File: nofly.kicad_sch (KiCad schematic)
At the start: 8 parts, among them J1 TYPE-C-31-M-12, J2 781710004, U1 USBLC6-2P6

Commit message: Finish wiring now?
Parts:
- J2: value 781710004 -> Conn_01x04_MountingPin; footprint acheron_Connectors:MOLEX_781710004 -> acheron_Connectors:MOLEX_PicoEZMate_781710004; symbol Connector_Generic:Conn_01x04 -> Connector_Generic_MountingPin:Conn_01x04_MountingPin
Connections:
- net GND: now also J2.MP (MountPin)
- no-connect marks 0 -> 2

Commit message: Some rerouting and checks
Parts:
- J2: value Conn_01x04_MountingPin -> 781710004
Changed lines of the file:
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@@
 		(dnp no)
 		(property "Reference" "R2"
-			(at 130.81 39.37 90)
+			(at 130.81 43.18 90)
 			(show_name no)
 			(do_not_autoplace no)
@@
 			(effects
 				(font
-					(size 0.508 0.508)
+					(size 0.762 0.762)
 				)
 			)
@@
 			)
 		)
-		(property "Value" "Conn_01x04_MountingPin"
-			(at 248.92 44.45 0)
-			(show_name no)
-			(do_not_autoplace no)
-			(effects
-				(font
-					(size 1.27 1.27)
-				)
-				(justify left)
-			)
-		)
+		(property "Value" "781710004"
+			(at 247.65 29.21 0)
+			(show_name no)
+			(do_not_autoplace no)
+			(effects
+				(font
+					(size 1.27 1.27)
+				)
+			)
+		)

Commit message: DRC ran, change EZM PN
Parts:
- J2: value 781710004 -> 781710004 / M1201RS-04-BK; LCSC Part Number C588524 -> C2840019; Manufacturer MOLEX -> XFCN
- U1: footprint Package_TO_SOT_SMD:SOT-666 -> Package_TO_SOT_SMD:SOT-563; LCSC Part Number C15999 -> C53059594; Manufacturer STMicroelectronics -> YTL
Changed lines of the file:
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@@
 			)
 		)
-		(property "Footprint" "Package_TO_SOT_SMD:SOT-666"
+		(property "Footprint" "Package_TO_SOT_SMD:SOT-563"
 			(at 183.134 49.911 0)
 			(hide yes)
@@
 			)
 		)
-		(property "Manufacturer" "STMicroelectronics"
+		(property "Manufacturer" "YTL"
 			(at 184.15 43.18 0)
 			(hide yes)
@@
 			)
 		)
-		(property "LCSC Part Number" "C15999"
+		(property "LCSC Part Number" "C53059594"
 			(at 184.15 43.18 0)
 			(hide yes)
@@
 			)
 		)
-		(property "Value" "781710004"
+		(property "Value" "781710004 / M1201RS-04-BK"
 			(at 247.65 29.21 0)
 			(show_name no)
@@
 			)
 		)
-		(property "Manufacturer" "MOLEX"
+		(property "Manufacturer" "XFCN"
 			(at 247.65 36.83 0)
 			(hide yes)
@@
 			)
 		)
-		(property "LCSC Part Number" "C588524"
+		(property "LCSC Part Number" "C2840019"
 			(at 247.65 36.83 0)
 			(hide yes)

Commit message: Remove visible silkscreen designators
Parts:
- R2: LCSC Part Number (none) -> C25905; Manufacturer (none) -> Uniroyal; Manufacturer Part Number (none) -> 0402WGF5101TCE
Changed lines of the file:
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@@
+			)
+		)
+		(property "LCSC Part Number" "C25905"
+			(at 130.81 41.275 90)
+			(hide yes)
+			(show_name no)
+			(do_not_autoplace no)
+			(effects
+				(font
+					(size 1.27 1.27)
+				)
+			)
+		)
+		(property "Manufacturer" "Uniroyal"
+			(at 130.81 41.275 90)
+			(hide yes)
+			(show_name no)
+			(do_not_autoplace no)
+			(effects
+				(font
+					(size 1.27 1.27)
+				)
+			)
+		)
+		(property "Manufacturer Part Number" "0402WGF5101TCE"
+			(at 130.81 41.275 90)
+			(hide yes)
+			(show_name no)
+			(do_not_autoplace no)
+			(effects
+				(font
+					(size 1.27 1.27)
+				)
 			)
 		)

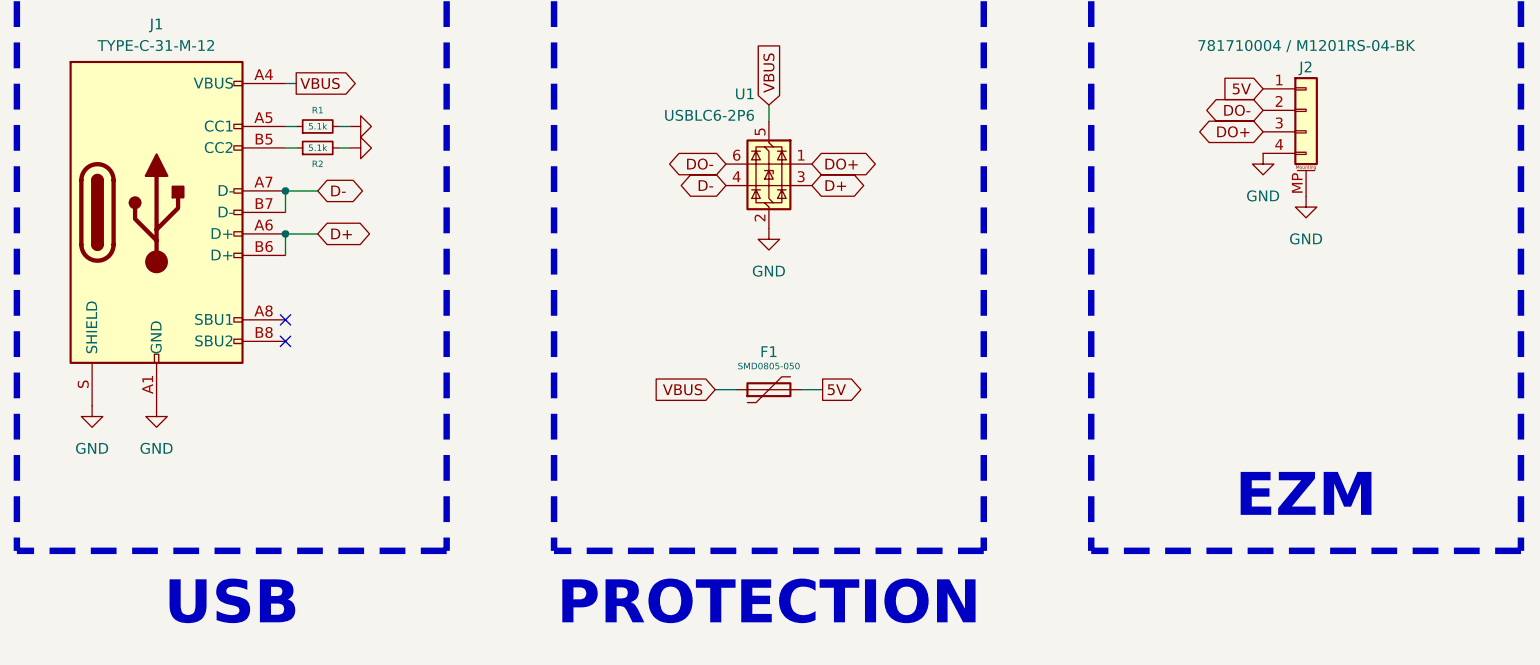
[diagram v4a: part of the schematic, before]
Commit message: Rotate ESD chip for clearance
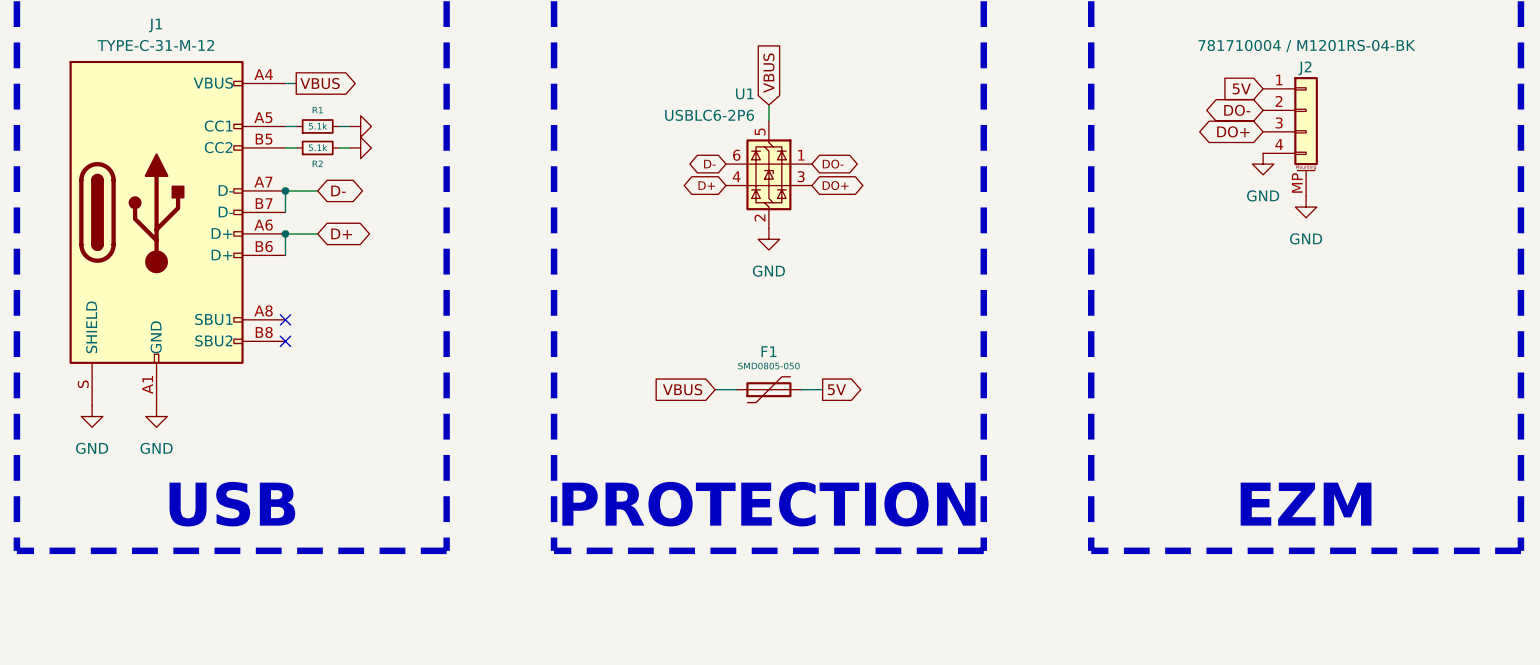
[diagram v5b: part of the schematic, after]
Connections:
- net D+: now also U1.4 (I/O2); no longer U1.3 (I/O2)
- net D-: now also U1.6 (I/O1); no longer U1.4 (I/O2)
- net DO+: now also U1.3 (I/O2); no longer U1.1 (I/O1)
- net DO-: now also U1.1 (I/O1); no longer U1.6 (I/O1)
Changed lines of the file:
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@@
 	(text "EZM"
 		(exclude_from_sim no)
-		(at 247.65 82.55 0)
+		(at 247.65 83.82 0)
 		(effects
 			(font
@@
 	(text "USB"
 		(exclude_from_sim no)
-		(at 120.65 95.25 0)
+		(at 120.65 83.82 0)
 		(effects
 			(font
@@
 	(text "PROTECTION"
 		(exclude_from_sim no)
-		(at 184.15 95.25 0)
+		(at 184.15 83.82 0)
 		(effects
 			(font
@@
 	(global_label "DO-"
 		(shape bidirectional)
-		(at 179.07 43.18 180)
-		(fields_autoplaced yes)
-		(effects
-			(font
-				(size 1.27 1.27)
-			)
-			(justify right)
-		)
-		(property "Intersheetrefs" "${INTERSHEET_REFS}"
-			(at 170.8006 43.18 0)
-			(hide yes)
-			(show_name no)
-			(do_not_autoplace no)
-			(effects
-				(font
-					(size 1.27 1.27)
-				)
-				(justify right)
+		(at 189.23 43.18 0)
+		(fields_autoplaced yes)
+		(effects
+			(font
+				(size 1.016 1.016)
+			)
+			(justify left)
+		)
+		(property "Intersheetrefs" "${INTERSHEET_REFS}"
+			(at 195.8452 43.18 0)
+			(hide yes)
+			(show_name no)
+			(do_not_autoplace no)
+			(effects
+				(font
+					(size 1.27 1.27)
+				)
+				(justify left)
 			)
 		)
@@
 	(global_label "D-"
 		(shape bidirectional)
-		(at 179.07 45.72 180)
-		(fields_autoplaced yes)
-		(effects
-			(font
-				(size 1.27 1.27)
+		(at 179.07 43.18 180)
+		(fields_autoplaced yes)
+		(effects
+			(font
+				(size 1.016 1.016)
 			)
 			(justify right)
 		)
 		(property "Intersheetrefs" "${INTERSHEET_REFS}"
-			(at 172.1311 45.72 0)
+			(at 173.5192 43.18 0)
 			(hide yes)
 			(show_name no)
@@
 	(global_label "D+"
 		(shape bidirectional)
-		(at 189.23 45.72 0)
-		(fields_autoplaced yes)
-		(effects
-			(font
-				(size 1.27 1.27)
-			)
-			(justify left)
-		)
-		(property "Intersheetrefs" "${INTERSHEET_REFS}"
-			(at 196.1689 45.72 0)
-			(hide yes)
-			(show_name no)
-			(do_not_autoplace no)
-			(effects
-				(font
-					(size 1.27 1.27)
-				)
-				(justify left)
+		(at 179.07 45.72 180)
+		(fields_autoplaced yes)
+		(effects
+			(font
+				(size 1.016 1.016)
+			)
+			(justify right)
+		)
+		(property "Intersheetrefs" "${INTERSHEET_REFS}"
+			(at 173.5192 45.72 0)
+			(hide yes)
+			(show_name no)
+			(do_not_autoplace no)
+			(effects
+				(font
+					(size 1.27 1.27)
+				)
+				(justify right)
 			)
 		)
@@
 	(global_label "DO+"
 		(shape bidirectional)
-		(at 189.23 43.18 0)
-		(fields_autoplaced yes)
-		(effects
-			(font
-				(size 1.27 1.27)
+		(at 189.23 45.72 0)
+		(fields_autoplaced yes)
+		(effects
+			(font
+				(size 1.016 1.016)
 			)
 			(justify left)
 		)
 		(property "Intersheetrefs" "${INTERSHEET_REFS}"
-			(at 197.4994 43.18 0)
-			(hide yes)
-			(show_name no)
+			(at 195.8452 45.72 0)
+			(hide yes)
+			(show_name no)

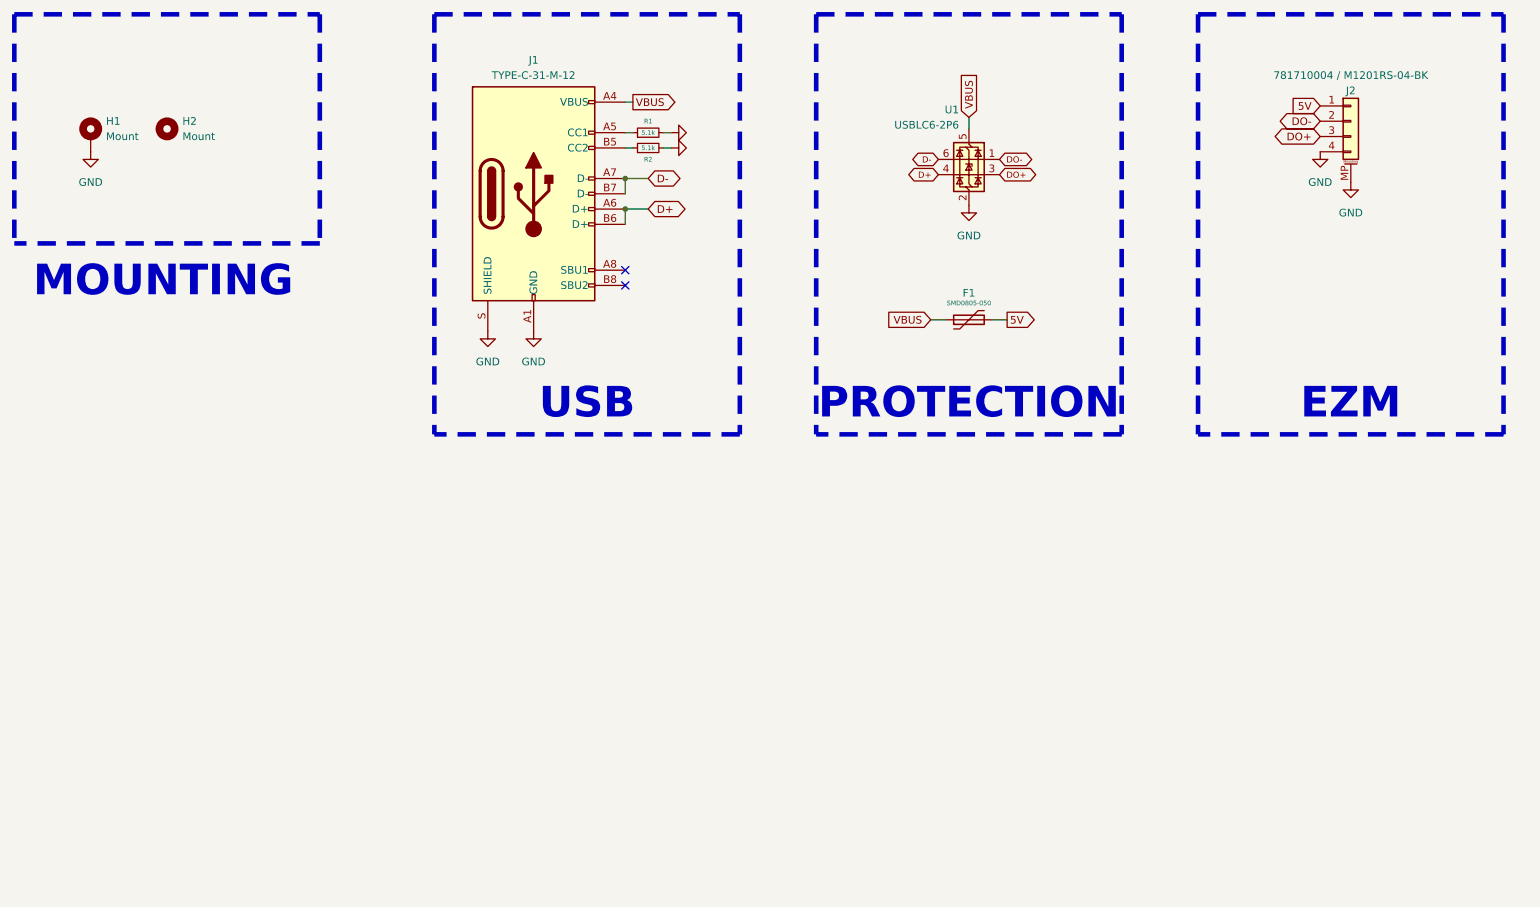
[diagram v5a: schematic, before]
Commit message: Add pannelization
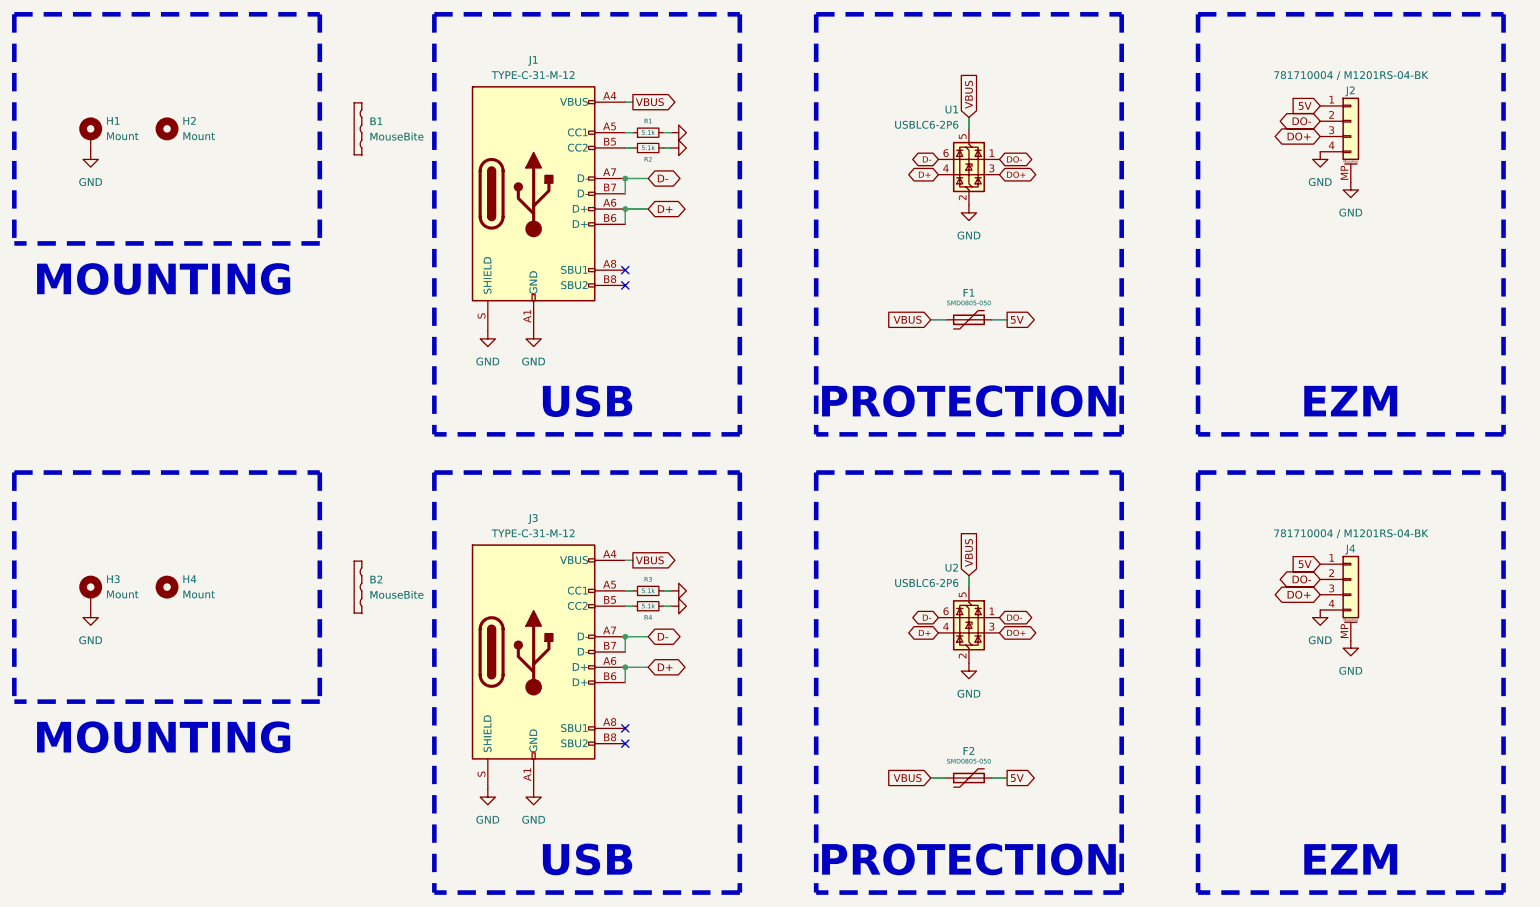
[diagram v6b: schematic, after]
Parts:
- added B1, B2: MouseBite, Panelization:MouseBite-Part_2.0x2.0mm_outset_D0.5mm_P0.85mm_3h, symbol Mechanical:MouseBite
- added F2: SMD0805-050, Fuse:Fuse_0805_2012Metric, symbol Device:Polyfuse
- added H3: Mount, MountingHole:MountingHole_2.2mm_M2_DIN965_Pad, symbol Mechanical:MountingHole_Pad_MP
- added H4: Mount, MountingHole:MountingHole_2.2mm_M2_DIN965_Pad, symbol Mechanical:MountingHole
- added J3: TYPE-C-31-M-12, acheron_Connectors:USB_C_Receptacle_Hroparts_TYPE-C-31-M-12, symbol Connector:USB_C_Receptacle_USB2.0_16P
- added J4: 781710004 / M1201RS-04-BK, acheron_Connectors:MOLEX_PicoEZMate_781710004, symbol Connector_Generic_MountingPin:Conn_01x04_MountingPin
- added R3, R4: 5.1k, Resistor_SMD:R_0402_1005Metric, symbol Device:R_Small
- added U2: USBLC6-2P6, Package_TO_SOT_SMD:SOT-563, symbol Power_Protection:USBLC6-2P6
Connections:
- net 5V: now also F2.2, J4.1 (Pin_1)
- net D+: now also J3.A6 (D+), J3.B6 (D+), U2.4 (I/O2)
- net D-: now also J3.A7 (D-), J3.B7 (D-), U2.6 (I/O1)
- net DO+: now also J4.3 (Pin_3), U2.3 (I/O2)
- net DO-: now also J4.2 (Pin_2), U2.1 (I/O1)
- net GND: now also H3.1 (MP), J3.A1 (GND), J3.A12 (GND), J3.B1 (GND), J3.B12 (GND), J3.S (SHIELD), J4.4 (Pin_4), J4.MP (MountPin), R3.2, R4.2, U2.2 (GND)
- net VBUS: now also F2.1, J3.A4 (VBUS), J3.A9 (VBUS), J3.B4 (VBUS), J3.B9 (VBUS), U2.5 (VBUS)
- new net: J3.A5 (CC1), R3.1
- new net: J3.B5 (CC2), R4.1
- no-connect marks 2 -> 4
